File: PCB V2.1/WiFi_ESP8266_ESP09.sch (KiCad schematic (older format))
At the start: 17 parts, among them IC1 ESP_09, P1 CONN_01X04, SW2 B3U-1000P, T1 1909763-1

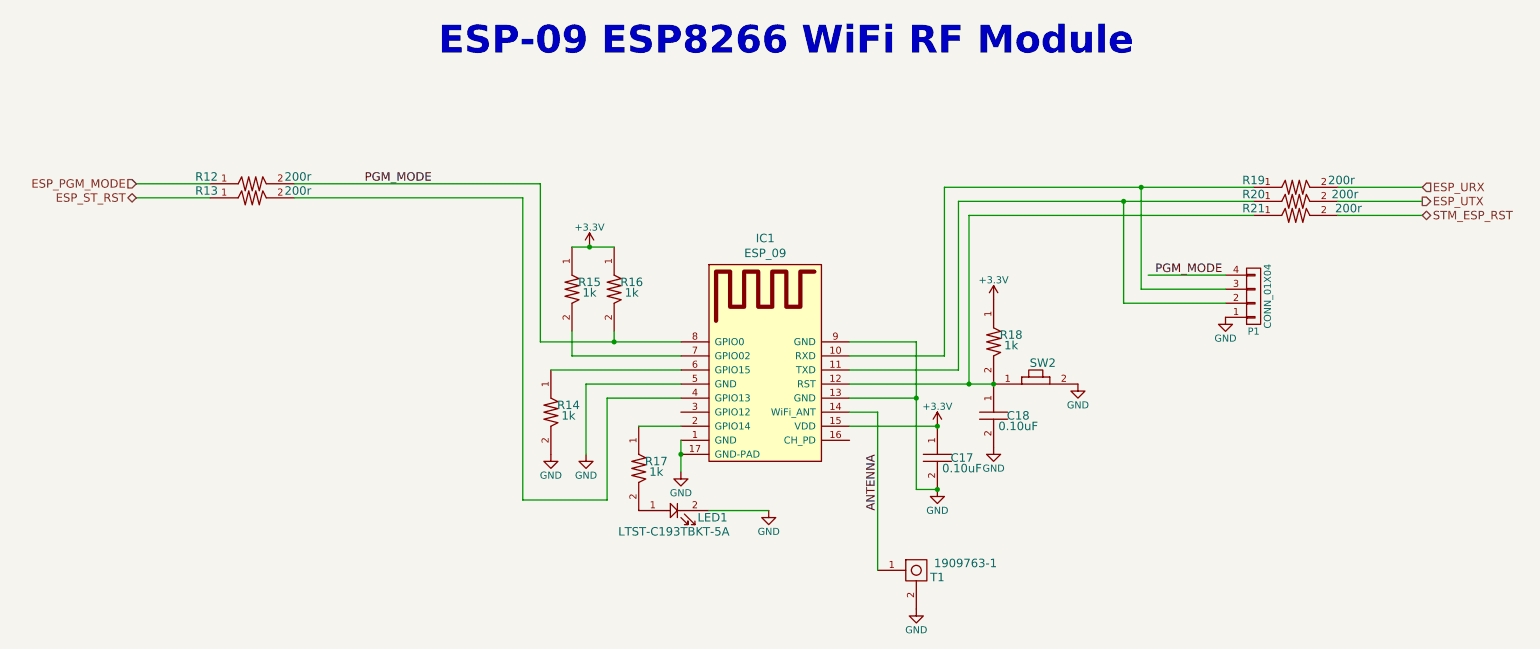
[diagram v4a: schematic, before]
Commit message: OTA
This commit contains adjustments to the schematics for over the air
update/programming of STM32 via the ESP8266 using its internal
bootloader. The two processors have been wired together to suppor this
fucntions, they can toggle reset of eachother and load firmware over
UART. Still deciding what reset signal pin on the STM32 to use fo rthis
purpose, next commit.
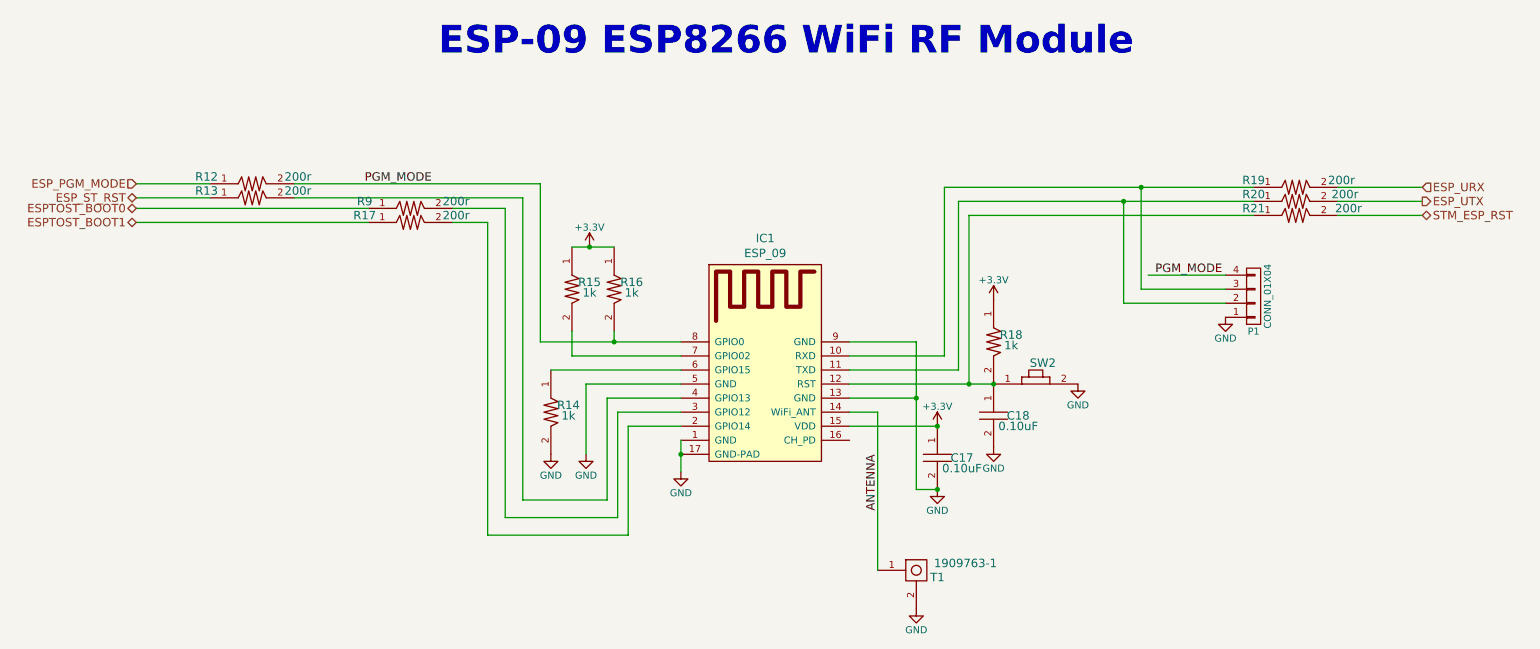
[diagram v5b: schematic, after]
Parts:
- removed LED1: LTST-C193TBKT-5A, PCB_Footprints:LED0603, symbol LTST-C193TBKT-5A
- removed R17: RC1005F102CS, PCB_Footprints:R0402, symbol RC1005F102CS
- added R17, R9: RC1005F201CS, PCB_Footprints:R0402, symbol RC1005F201CS
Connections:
- net at IC1.2 (GPIO14): now also R17.2
- net at IC1.3 (GPIO12): now also R9.2
- new net ESPTOST_BOOT0: R9.1
- new net ESPTOST_BOOT1: R17.1
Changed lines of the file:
@@
 LIBS:HydroPWNics_Lib
 LIBS:ESP32-footprints-Shem-Lib
+LIBS:ESP8266
 LIBS:SunLeaf_V2-cache
 EELAYER 25 0
@@
 $EndComp
 $Comp
-L GND #PWR26
+L GND #PWR020
 U 1 1 57D74187
 P 7050 4300
-F 0 "#PWR26" H 7050 4050 50  0001 C CNN
+F 0 "#PWR020" H 7050 4050 50  0001 C CNN
 F 1 "GND" H 7050 4150 50  0000 C CNN
 F 2 "" H 7050 4300 50  0000 C CNN
@@
 $EndComp
 $Comp
-L GND #PWR29
+L GND #PWR021
 U 1 1 57D744DC
 P 8050 3550
-F 0 "#PWR29" H 8050 3300 50  0001 C CNN
+F 0 "#PWR021" H 8050 3300 50  0001 C CNN
 F 1 "GND" H 8050 3400 50  0000 C CNN
 F 2 "" H 8050 3550 50  0000 C CNN
@@
 $EndComp
 $Comp
-L GND #PWR28
+L GND #PWR022
 U 1 1 57D745DC
 P 7450 4000
-F 0 "#PWR28" H 7450 3750 50  0001 C CNN
+F 0 "#PWR022" H 7450 3750 50  0001 C CNN
 F 1 "GND" H 7450 3850 50  0000 C CNN
 F 2 "" H 7450 4000 50  0000 C CNN
@@
 $EndComp
 $Comp
-L GND #PWR24
+L GND #PWR023
 U 1 1 57D74617
 P 6900 5150
-F 0 "#PWR24" H 6900 4900 50  0001 C CNN
+F 0 "#PWR023" H 6900 4900 50  0001 C CNN
 F 1 "GND" H 6900 5000 50  0000 C CNN
 F 2 "" H 6900 5150 50  0000 C CNN
@@
 $EndComp
 $Comp
-L +3.3V #PWR27
+L +3.3V #PWR024
 U 1 1 57D7466A
 P 7450 2950
-F 0 "#PWR27" H 7450 2800 50  0001 C CNN
+F 0 "#PWR024" H 7450 2800 50  0001 C CNN
 F 1 "+3.3V" H 7450 3090 50  0000 C CNN
 F 2 "" H 7450 2950 50  0000 C CNN
@@
 $EndComp
 $Comp
-L GND #PWR19
+L GND #PWR025
 U 1 1 57D76DFD
 P 4300 4050
-F 0 "#PWR19" H 4300 3800 50  0001 C CNN
+F 0 "#PWR025" H 4300 3800 50  0001 C CNN
 F 1 "GND" H 4300 3900 50  0000 C CNN
 F 2 "" H 4300 4050 50  0000 C CNN
@@
 $EndComp
 $Comp
-L GND #PWR22
+L GND #PWR026
 U 1 1 57D76E32
 P 5225 4175
-F 0 "#PWR22" H 5225 3925 50  0001 C CNN
+F 0 "#PWR026" H 5225 3925 50  0001 C CNN
 F 1 "GND" H 5225 4025 50  0000 C CNN
 F 2 "" H 5225 4175 50  0000 C CNN
@@
 $EndComp
 $Comp
-L GND #PWR20
+L GND #PWR027
 U 1 1 57D76FA5
 P 4550 4050
-F 0 "#PWR20" H 4550 3800 50  0001 C CNN
+F 0 "#PWR027" H 4550 3800 50  0001 C CNN
 F 1 "GND" H 4550 3900 50  0000 C CNN
 F 2 "" H 4550 4050 50  0000 C CNN
@@
 $EndComp
 $Comp
-L +3.3V #PWR21
+L +3.3V #PWR028
 U 1 1 57D77481
 P 4575 2575
-F 0 "#PWR21" H 4575 2425 50  0001 C CNN
+F 0 "#PWR028" H 4575 2425 50  0001 C CNN
 F 1 "+3.3V" H 4575 2715 50  0000 C CNN
 F 2 "" H 4575 2575 50  0000 C CNN
 F 3 "" H 4575 2575 50  0000 C CNN
 	1    4575 2575
-	1    0    0    -1
-$EndComp
-$Comp
-L LTST-C193TBKT-5A LED1
-U 1 1 57D796B9
-P 5175 4450
-F 0 "LED1" H 5450 4400 60  0000 C CNN
-F 1 "LTST-C193TBKT-5A" H 5175 4300 60  0000 C CNN
-F 2 "PCB_Footprints:LED0603" H 6600 6375 60  0001 C CNN
-F 3 "http://optoelectronics.liteon.com/upload/download/DS22-2004-060/P_100_LTST-C193TBKT-5A.pdf" H 6800 6500 60  0001 C CNN
-F 4 "0.06102 @ 6000" H 5025 4650 60  0001 C CNN "Cost"
-F 5 "8 Sept 2016" H 5125 4750 60  0001 C CNN "Date Created"
-F 6 "8 Sept 2016" H 5225 4850 60  0001 C CNN "Date Modified"
-F 7 "Adam Vadala-Roth" H 5325 4950 60  0001 C CNN "Designer"
-F 8 "0.55mm" H 5425 5050 60  0001 C CNN "Height"
-F 9 "Yes" H 5525 5150 60  0001 C CNN "RhoS?"
-F 10 "Lite-On Inc" H 5625 5250 60  0001 C CNN "MFR"
-F 11 "LTST-C193TBKT-5A" H 5725 5350 60  0001 C CNN "MFR#"
-F 12 "SMT/SMD" H 5825 5450 60  0001 C CNN "Mounting"
-F 13 "2" H 5925 5550 60  0001 C CNN "Pin Count#"
-F 14 "Active" H 6025 5650 60  0001 C CNN "Status"
-F 15 "N/A" H 6125 5750 60  0001 C CNN "Tolerance"
-F 16 "0603 LED" H 6225 5850 60  0001 C CNN "Type"
-F 17 "2.8V Forward Voltage" H 6325 5950 60  0001 C CNN "Voltage"
-F 18 "N/A" H 6425 6050 60  0001 C CNN "Wattage"
-F 19 "N/A" H 6525 6150 60  0001 C CNN "Component-Value"
-F 20 "Blue 470nm LED Indication - Discrete 2.8V 0603 (1608 Metric)" H 6625 6250 60  0001 C CNN "Description"
-	1    5175 4450
-	1    0    0    -1
-$EndComp
-$Comp
-L RC1005F102CS R17
-U 1 1 57D79AD8
-P 4925 4150
-F 0 "R17" V 4875 4275 60  0000 C CNN
-F 1 "RC1005F102CS" H 4925 4000 60  0001 C CNN
-F 2 "PCB_Footprints:R0402" H 4525 4400 60  0001 C CNN
-F 3 "https://media.digikey.com/pdf/Data%20Sheets/Samsung%20PDFs/RC_Series_ds.pdf" H 4625 4600 60  0001 C CNN
-F 4 "0.00173 @ 5000" H 6475 6100 60  0001 C CNN "Cost"
-F 5 "5 Sept 2016" H 4825 4700 60  0001 C CNN "Date Created"
-F 6 "5 Sept 2016" H 4925 4800 60  0001 C CNN "Date Modified"
-F 7 "Adam Vadala-Roth" H 5025 4900 60  0001 C CNN "Designer"
-F 8 "0.4mm" H 5125 5000 60  0001 C CNN "Height"
-F 9 "Yes" H 5225 5100 60  0001 C CNN "RHoS?"
-F 10 "Samsung Electro-Mechanics America, Inc." H 5325 5200 60  0001 C CNN "MFR"
-F 11 "RC1005F102CS" H 5425 5300 60  0001 C CNN "MFR#"
-F 12 "SMT/SMD" H 5525 5400 60  0001 C CNN "Mounting"
-F 13 "2" H 5625 5500 60  0001 C CNN "Pin Count#"
-F 14 "Active" H 5725 5600 60  0001 C CNN "Status"
-F 15 "%" H 5825 5700 60  0001 C CNN "Tolerance"
-F 16 "passive" H 5925 5800 60  0001 C CNN "Type"
-F 17 "N/A" H 6025 5900 60  0001 C CNN "Voltage"
-F 18 "1/16" H 6125 6000 60  0001 C CNN "Wattage"
-F 19 "1k" V 4950 4275 60  0000 C CNN "Component-Value"
-F 20 "RES SMD 1K OHM 1% 1/16W 0402" H 6325 6200 60  0001 C CNN "Description"
-	1    4925 4150
-	0    1    1    0
-$EndComp
-$Comp
-L GND #PWR23
-U 1 1 57D7A082
-P 5850 4450
-F 0 "#PWR23" H 5850 4200 50  0001 C CNN
-F 1 "GND" H 5850 4300 50  0000 C CNN
-F 2 "" H 5850 4450 50  0000 C CNN
-F 3 "" H 5850 4450 50  0000 C CNN
-	1    5850 4450
 	1    0    0    -1
 $EndComp
@@
 $EndComp
 $Comp
-L GND #PWR30
+L GND #PWR029
 U 1 1 57D7BD68
 P 9100 3075
-F 0 "#PWR30" H 9100 2825 50  0001 C CNN
+F 0 "#PWR029" H 9100 2825 50  0001 C CNN
 F 1 "GND" H 9100 2925 50  0000 C CNN
 F 2 "" H 9100 3075 50  0000 C CNN
@@
 ESP-09 ESP8266 WiFi RF Module
 $Comp
-L +3.3V #PWR25
+L +3.3V #PWR030
 U 1 1 57D94D09
 P 7050 3850
-F 0 "#PWR25" H 7050 3700 50  0001 C CNN
+F 0 "#PWR030" H 7050 3700 50  0001 C CNN
 F 1 "+3.3V" H 7050 3990 50  0000 C CNN
 F 2 "" H 7050 3850 50  0000 C CNN
@@
 Wire Wire Line
 	9100 2875 8500 2875
-Wire Wire Line
-	5225 3850 4925 3850
-Wire Wire Line
-	5850 4450 5425 4450
 Connection ~ 4575 2575
 Wire Wire Line
@@
 Wire Wire Line
 	6425 3850 7050 3850
+Text HLabel 1350 2300 0    60   BiDi ~ 0
+ESPTOST_BOOT0
+Text HLabel 1350 2400 0    60   BiDi ~ 0
+ESPTOST_BOOT1
+Wire Wire Line
+	5225 3750 4775 3750
+Wire Wire Line
+	4775 3750 4775 4500
+Wire Wire Line
+	4775 4500 3975 4500
+Wire Wire Line
+	3975 4500 3975 2300
+Wire Wire Line
+	5225 3850 4850 3850
+Wire Wire Line
+	4850 3850 4850 4625
+Wire Wire Line
+	3850 4625 4850 4625
+Wire Wire Line
+	3850 2400 3850 4625
+$Comp
+L RC1005F201CS R9
+U 1 1 57DFC0D1
+P 3300 2300
+F 0 "R9" H 2975 2350 60  0000 C CNN
+F 1 "RC1005F201CS" H 3300 2150 60  0001 C CNN
+F 2 "PCB_Footprints:R0402" H 2900 2550 60  0001 C CNN
+F 3 "https://media.digikey.com/pdf/Data%20Sheets/Samsung%20PDFs/RC_Series_ds.pdf" H 3000 2750 60  0001 C CNN
+F 4 "0.00257 @ 5000" H 4850 4250 60  0001 C CNN "Cost"
+F 5 "5 Sept 2016" H 3200 2850 60  0001 C CNN "Date Created"
+F 6 "5 Sept 2016" H 3300 2950 60  0001 C CNN "Date Modified"
+F 7 "Adam Vadala-Roth" H 3400 3050 60  0001 C CNN "Designer"
+F 8 "0.4mm" H 3500 3150 60  0001 C CNN "Height"
+F 9 "Yes" H 3600 3250 60  0001 C CNN "RHoS?"
+F 10 "Samsung Electro-Mechanics America, Inc." H 3700 3350 60  0001 C CNN "MFR"
+F 11 "RC1005F201CS" H 3800 3450 60  0001 C CNN "MFR#"
+F 12 "SMT/SMD" H 3900 3550 60  0001 C CNN "Mounting"
+F 13 "2" H 4000 3650 60  0001 C CNN "Pin Count#"
+F 14 "Active" H 4100 3750 60  0001 C CNN "Status"
+F 15 "1%" H 4200 3850 60  0001 C CNN "Tolerance"
+F 16 "passive" H 4300 3950 60  0001 C CNN "Type"
+F 17 "N/A" H 4400 4050 60  0001 C CNN "Voltage"
+F 18 "1/16" H 4500 4150 60  0001 C CNN "Wattage"
+F 19 "200r" H 3625 2350 60  0000 C CNN "Component-Value"
+F 20 "RES SMD 200 OHM 1% 1/16W 0402" H 4700 4350 60  0001 C CNN "Description"
+	1    3300 2300
+	1    0    0    -1
+$EndComp
+$Comp
+L RC1005F201CS R17
+U 1 1 57DFC174
+P 3300 2400
+F 0 "R17" H 2975 2450 60  0000 C CNN
+F 1 "RC1005F201CS" H 3300 2250 60  0001 C CNN
+F 2 "PCB_Footprints:R0402" H 2900 2650 60  0001 C CNN
+F 3 "https://media.digikey.com/pdf/Data%20Sheets/Samsung%20PDFs/RC_Series_ds.pdf" H 3000 2850 60  0001 C CNN
+F 4 "0.00257 @ 5000" H 4850 4350 60  0001 C CNN "Cost"
+F 5 "5 Sept 2016" H 3200 2950 60  0001 C CNN "Date Created"
+F 6 "5 Sept 2016" H 3300 3050 60  0001 C CNN "Date Modified"
+F 7 "Adam Vadala-Roth" H 3400 3150 60  0001 C CNN "Designer"
+F 8 "0.4mm" H 3500 3250 60  0001 C CNN "Height"
+F 9 "Yes" H 3600 3350 60  0001 C CNN "RHoS?"
+F 10 "Samsung Electro-Mechanics America, Inc." H 3700 3450 60  0001 C CNN "MFR"
+F 11 "RC1005F201CS" H 3800 3550 60  0001 C CNN "MFR#"
+F 12 "SMT/SMD" H 3900 3650 60  0001 C CNN "Mounting"
+F 13 "2" H 4000 3750 60  0001 C CNN "Pin Count#"
+F 14 "Active" H 4100 3850 60  0001 C CNN "Status"
+F 15 "1%" H 4200 3950 60  0001 C CNN "Tolerance"
+F 16 "passive" H 4300 4050 60  0001 C CNN "Type"
+F 17 "N/A" H 4400 4150 60  0001 C CNN "Voltage"
+F 18 "1/16" H 4500 4250 60  0001 C CNN "Wattage"
+F 19 "200r" H 3625 2450 60  0000 C CNN "Component-Value"
+F 20 "RES SMD 200 OHM 1% 1/16W 0402" H 4700 4450 60  0001 C CNN "Description"
+	1    3300 2400
+	1    0    0    -1
+$EndComp
+Wire Wire Line
+	3000 2300 1350 2300
+Wire Wire Line
+	3000 2400 1350 2400
+Wire Wire Line
+	3600 2400 3850 2400
+Wire Wire Line
+	3975 2300 3600 2300
 $EndSCHEMATC

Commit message: App Notes
App notes added to datasheets folder.
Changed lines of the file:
@@
 $EndComp
 $Comp
-L GND #PWR27
+L GND #PWR022
 U 1 1 57D74187
 P 7050 4300
-F 0 "#PWR27" H 7050 4050 50  0001 C CNN
+F 0 "#PWR022" H 7050 4050 50  0001 C CNN
 F 1 "GND" H 7050 4150 50  0000 C CNN
 F 2 "" H 7050 4300 50  0000 C CNN
@@
 $EndComp
 $Comp
-L GND #PWR30
+L GND #PWR023
 U 1 1 57D744DC
 P 8050 3550
-F 0 "#PWR30" H 8050 3300 50  0001 C CNN
+F 0 "#PWR023" H 8050 3300 50  0001 C CNN
 F 1 "GND" H 8050 3400 50  0000 C CNN
 F 2 "" H 8050 3550 50  0000 C CNN
@@
 $EndComp
 $Comp
-L GND #PWR29
+L GND #PWR024
 U 1 1 57D745DC
 P 7450 4000
-F 0 "#PWR29" H 7450 3750 50  0001 C CNN
+F 0 "#PWR024" H 7450 3750 50  0001 C CNN
 F 1 "GND" H 7450 3850 50  0000 C CNN
 F 2 "" H 7450 4000 50  0000 C CNN
@@
 $EndComp
 $Comp
-L GND #PWR25
+L GND #PWR025
 U 1 1 57D74617
 P 6900 5150
-F 0 "#PWR25" H 6900 4900 50  0001 C CNN
+F 0 "#PWR025" H 6900 4900 50  0001 C CNN
 F 1 "GND" H 6900 5000 50  0000 C CNN
 F 2 "" H 6900 5150 50  0000 C CNN
@@
 $EndComp
 $Comp
-L +3.3V #PWR28
+L +3.3V #PWR026
 U 1 1 57D7466A
 P 7450 2950
-F 0 "#PWR28" H 7450 2800 50  0001 C CNN
+F 0 "#PWR026" H 7450 2800 50  0001 C CNN
 F 1 "+3.3V" H 7450 3090 50  0000 C CNN
 F 2 "" H 7450 2950 50  0000 C CNN
@@
 $EndComp
 $Comp
-L GND #PWR21
+L GND #PWR027
 U 1 1 57D76DFD
 P 4300 4050
-F 0 "#PWR21" H 4300 3800 50  0001 C CNN
+F 0 "#PWR027" H 4300 3800 50  0001 C CNN
 F 1 "GND" H 4300 3900 50  0000 C CNN
 F 2 "" H 4300 4050 50  0000 C CNN
@@
 $EndComp
 $Comp
-L GND #PWR24
+L GND #PWR028
 U 1 1 57D76E32
 P 5225 4175
-F 0 "#PWR24" H 5225 3925 50  0001 C CNN
+F 0 "#PWR028" H 5225 3925 50  0001 C CNN
 F 1 "GND" H 5225 4025 50  0000 C CNN
 F 2 "" H 5225 4175 50  0000 C CNN
@@
 $EndComp
 $Comp
-L GND #PWR22
+L GND #PWR029
 U 1 1 57D76FA5
 P 4550 4050
-F 0 "#PWR22" H 4550 3800 50  0001 C CNN
+F 0 "#PWR029" H 4550 3800 50  0001 C CNN
 F 1 "GND" H 4550 3900 50  0000 C CNN
 F 2 "" H 4550 4050 50  0000 C CNN
@@
 $EndComp
 $Comp
-L +3.3V #PWR23
+L +3.3V #PWR030
 U 1 1 57D77481
 P 4575 2575
-F 0 "#PWR23" H 4575 2425 50  0001 C CNN
+F 0 "#PWR030" H 4575 2425 50  0001 C CNN
 F 1 "+3.3V" H 4575 2715 50  0000 C CNN
 F 2 "" H 4575 2575 50  0000 C CNN
@@
 $EndComp
 $Comp
-L GND #PWR31
+L GND #PWR031
 U 1 1 57D7BD68
 P 9100 3075
-F 0 "#PWR31" H 9100 2825 50  0001 C CNN
+F 0 "#PWR031" H 9100 2825 50  0001 C CNN
 F 1 "GND" H 9100 2925 50  0000 C CNN
 F 2 "" H 9100 3075 50  0000 C CNN
@@
 ESP-09 ESP8266 WiFi RF Module
 $Comp
-L +3.3V #PWR26
+L +3.3V #PWR032
 U 1 1 57D94D09
 P 7050 3850
-F 0 "#PWR26" H 7050 3700 50  0001 C CNN
+F 0 "#PWR032" H 7050 3700 50  0001 C CNN
 F 1 "+3.3V" H 7050 3990 50  0000 C CNN
 F 2 "" H 7050 3850 50  0000 C CNN
@@
 	4850 3850 4850 4625
 Wire Wire Line
-	3850 4625 4850 4625
-Wire Wire Line
-	3850 2400 3850 4625
+	4850 4625 3850 4625
+Wire Wire Line
+	3850 4625 3850 2400
 $Comp
 L RC1005F201CS R9
@@
 	3000 2400 1350 2400
 Wire Wire Line
-	3600 2400 3850 2400
+	3850 2400 3600 2400
 Wire Wire Line
 	3975 2300 3600 2300
